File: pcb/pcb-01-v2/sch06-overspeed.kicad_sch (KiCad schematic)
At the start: 37 parts, among them J3 B3B-PH-K-S(LF)(SN), Q3 2N7002K-7, U4 TPS7A1601ADGNR, U8 LM2907M-14/NOPB, U9 TLV1701AIDBVR

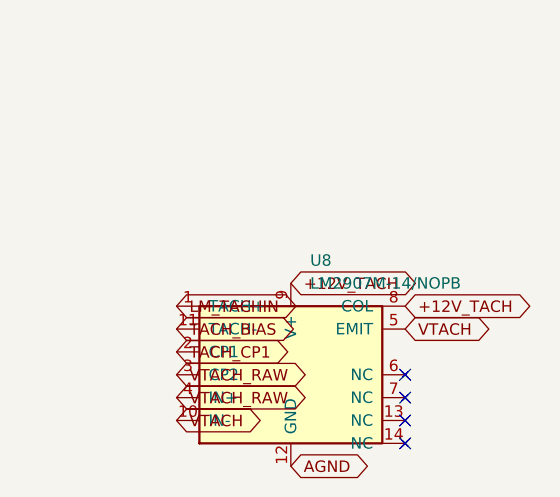
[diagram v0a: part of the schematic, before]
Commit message: Finalize PCB-01 V2 JLC submission package
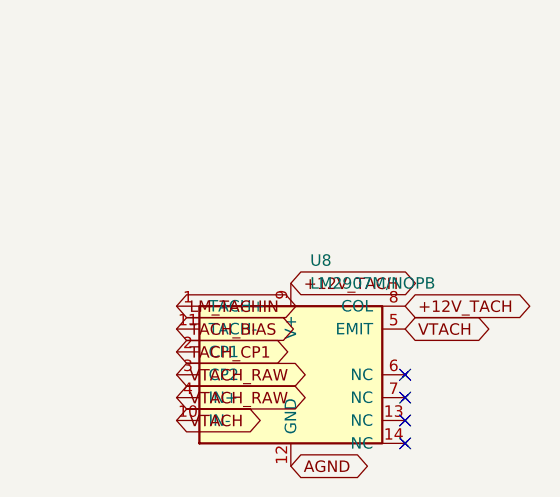
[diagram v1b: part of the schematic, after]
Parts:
- U8: value LM2907M-14/NOPB -> LM2907M/NOPB
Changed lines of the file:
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@@
 			)
 		)
-		(property "Value" "LM2907M-14/NOPB"
+		(property "Value" "LM2907M/NOPB"
 			(at 206.6133 212.09 0)
 			(show_name no)
